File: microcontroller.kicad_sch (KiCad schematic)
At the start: 1 part, among them U3 STM32H743VITx

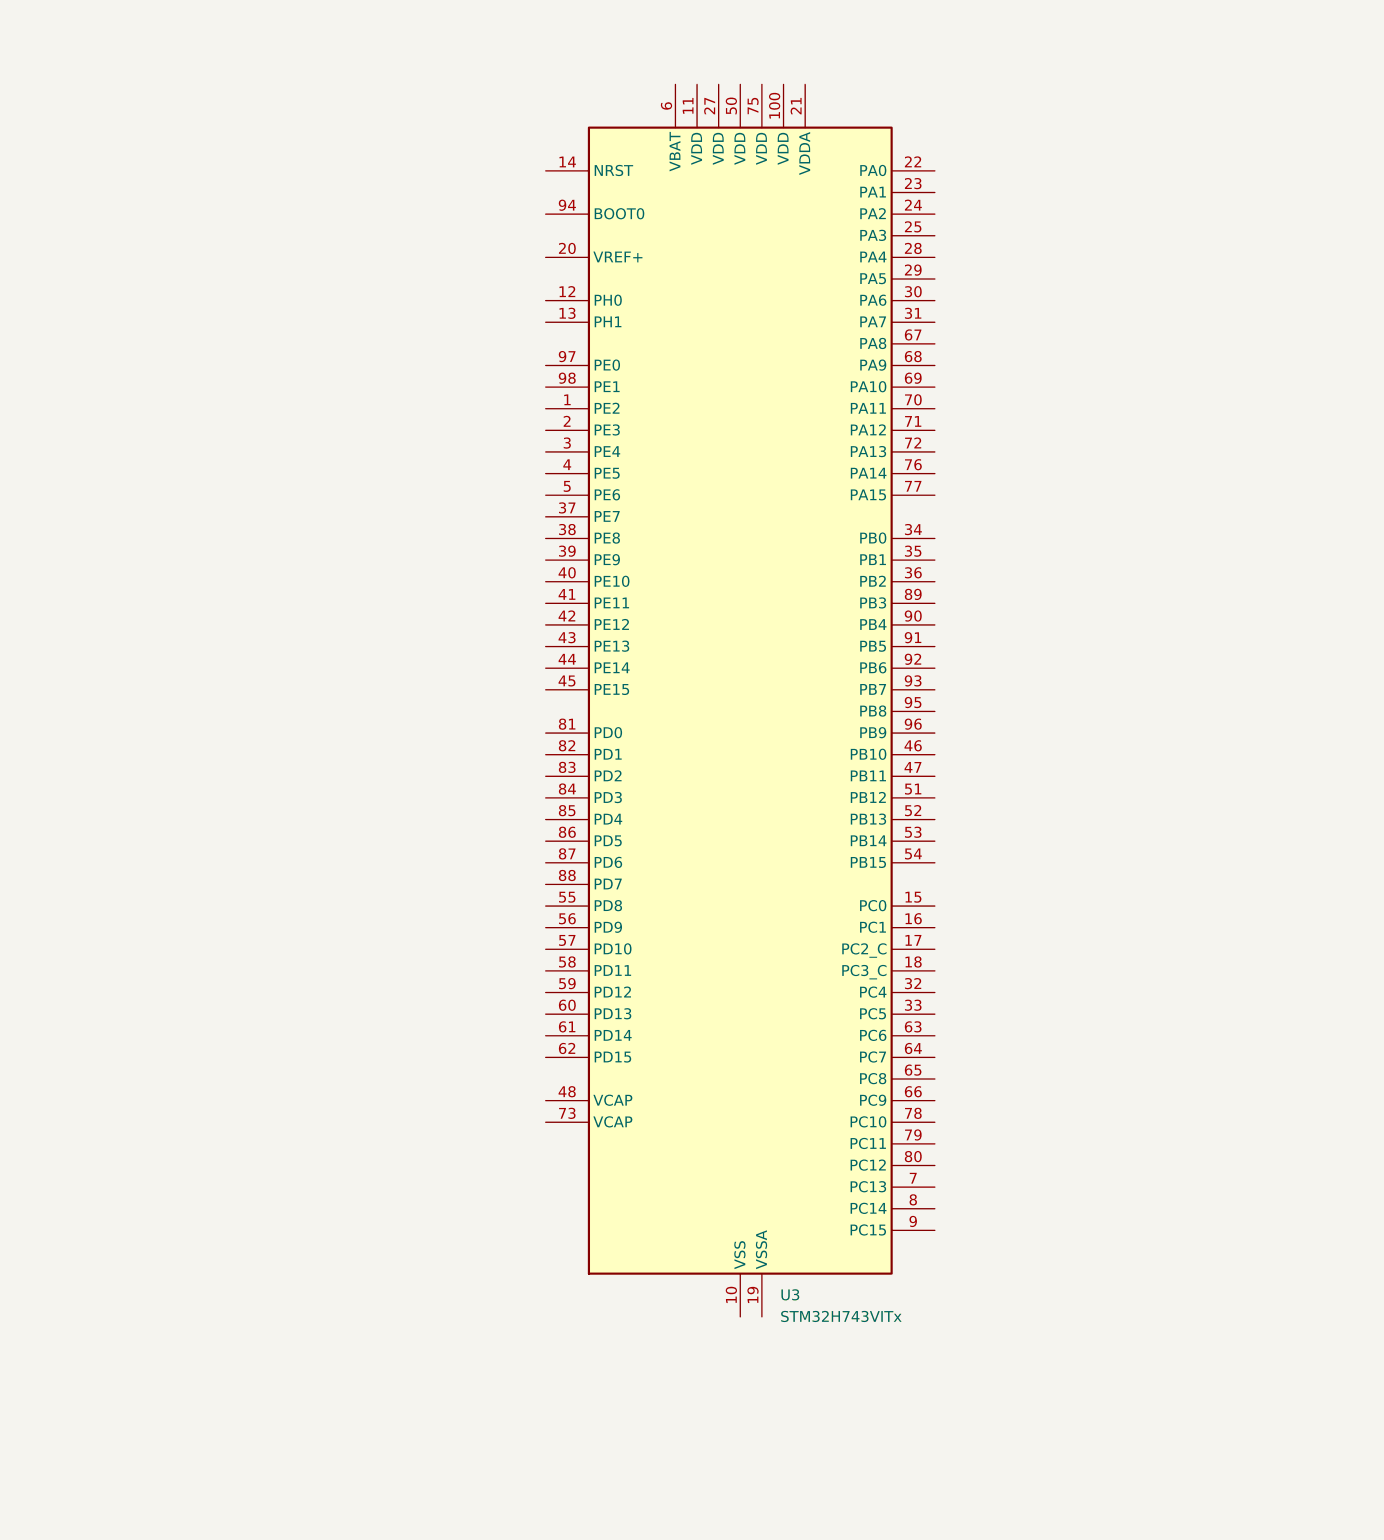
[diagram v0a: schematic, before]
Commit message: Added the power and gnd connections, decoupling capacitors and the reset circuit. Need to finish clock/oscillator, boot configuration, and programming interface schematics.
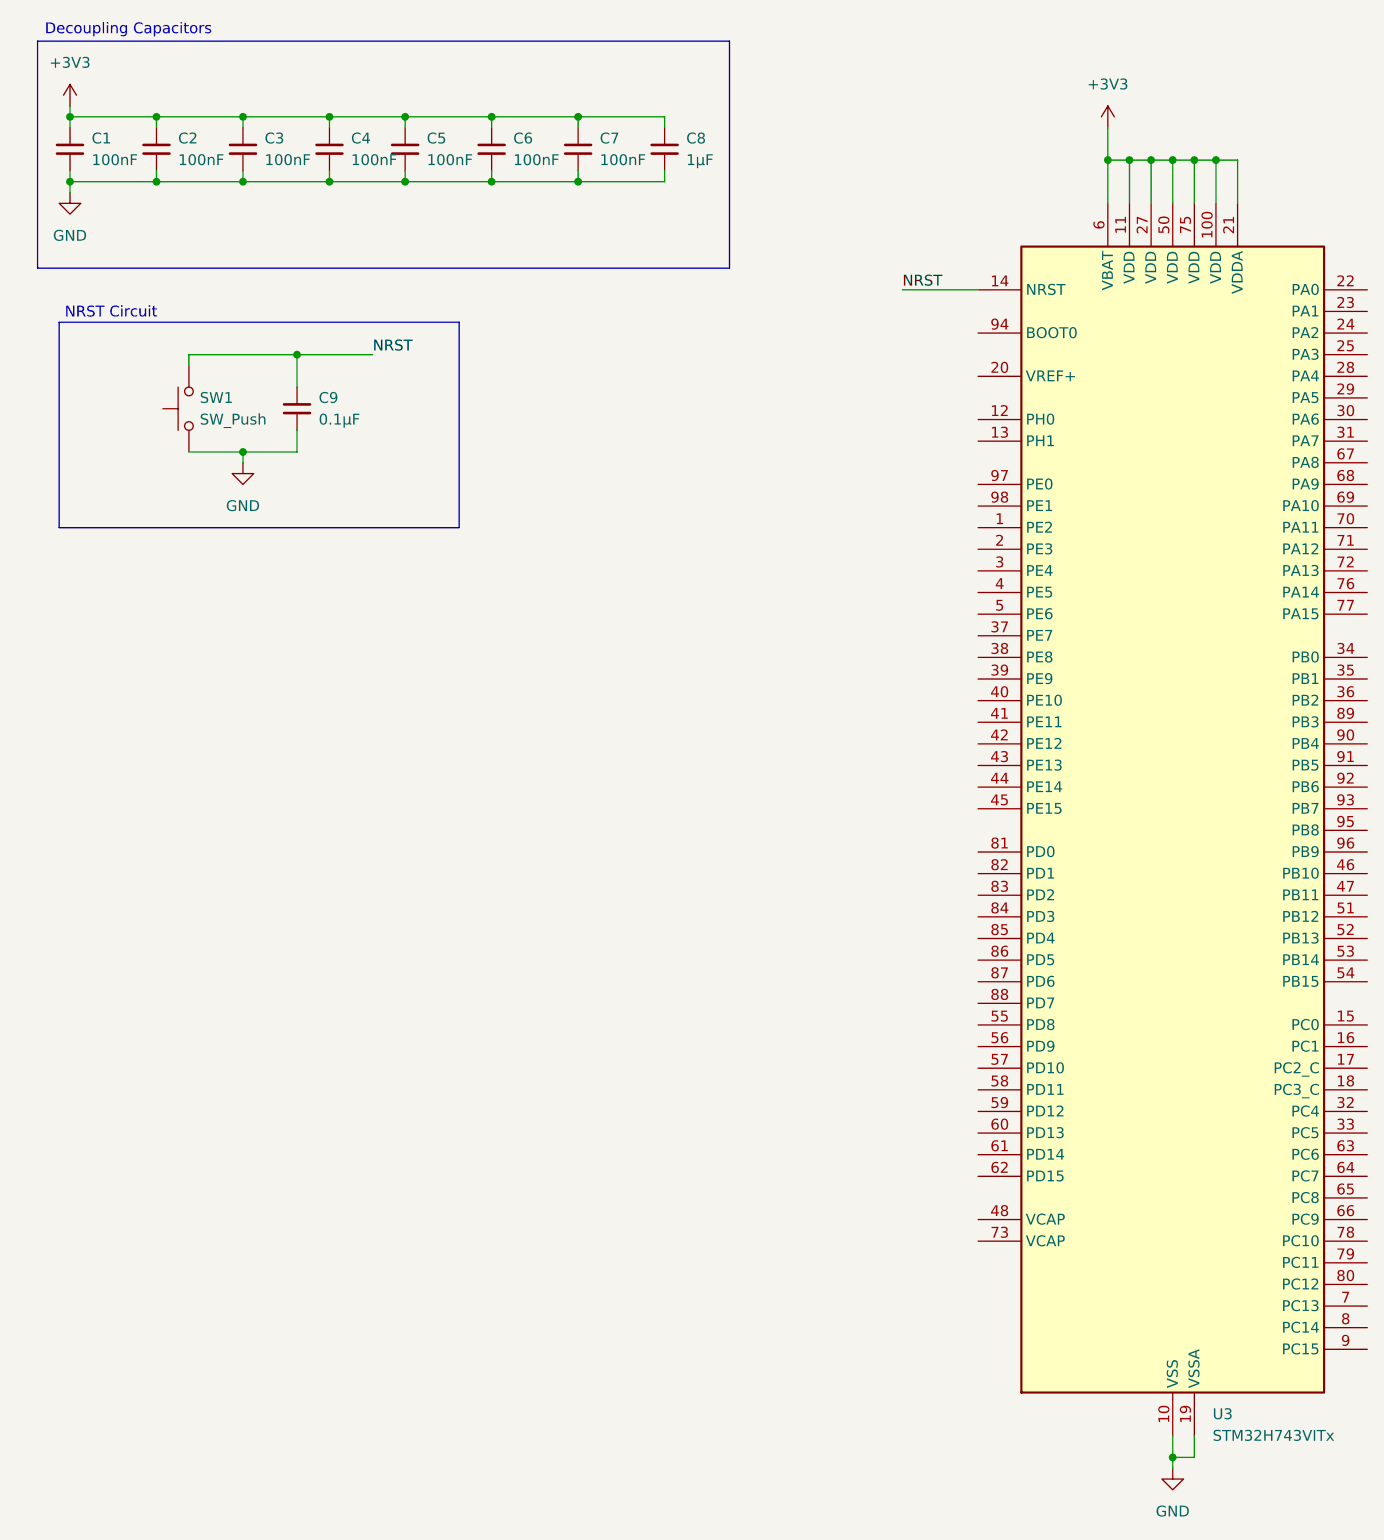
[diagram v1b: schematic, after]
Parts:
- added C1, C2, C3, C4, C5, C6, C7: 100nF, symbol Device:C_Small
- added C8: 1μF, symbol Device:C_Small
- added C9: 0.1μF, Converter_DCDC:Converter_DCDC_RECOM_R-78S-0.1_THT, symbol Device:C_Small
- added SW1: SW_Push, Package_DIP:DIP-24_W7.62mm, symbol Switch:SW_Push
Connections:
- net GND: now reaches U3.10 (VSS), U3.26 (VSS), U3.49 (VSS), U3.74 (VSS), U3.99 (VSS)
- net GND: now also U3.19 (VSSA), C1.2, C2.2, C3.2, C4.2, C5.2, C6.2, C7.2, C8.2, C9.2, SW1.1
- net +3V3: now reaches U3.100 (VDD)
- net +3V3: now also U3.11 (VDD), U3.21 (VDDA), U3.27 (VDD), U3.50 (VDD), U3.6 (VBAT), U3.75 (VDD), C1.1, C2.1, C3.1, C4.1, C5.1, C6.1, C7.1, C8.1
- net at U3.14 (NRST): no longer names the net of U3.14 (NRST)
- net at U3.14 (NRST): now also C9.1, SW1.2
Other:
- note added: "Decoupling Capacitors"
- note added: "NRST Circuit"
- moved on the sheet: U3
